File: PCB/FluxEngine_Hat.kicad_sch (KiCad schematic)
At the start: 6 parts, among them J1 CY8CKIT-059, P1 FDD_IBMPC_host, P2 FDD_SA800_host

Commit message: CDC pinouts
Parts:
- removed P1: FDD_IBMPC_host, 000_LOCAL:IDC-Header_2x17_P2.54mm_Latch_Vertical - FDD, symbol 000_LOCAL:FDD_IBMPC_host
- added P1: FDC_BUS_IBMPC, 000_LOCAL:IDC-Header_2x17_P2.54mm_Latch_Vertical - FDD, symbol 000_LOCAL:FDC_BUS_IBMPC
- P2: value FDD_SA800_host -> FDC_BUS_SA851; symbol 000_LOCAL:FDD_SA800_host -> 000_LOCAL:FDC_BUS_SA851
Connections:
- net DIR: now also P1.18 (DIR)
- net GND: now also P1.1 (GND), P1.11 (GND), P1.13 (GND), P1.15 (GND), P1.17 (GND), P1.19 (GND), P1.21 (GND), P1.23 (GND), P1.25 (GND), P1.27 (GND), P1.29 (GND), P1.31 (GND), P1.33 (GND), P1.7 (GND), P1.9 (GND)
- net SIDE: now also P1.32 (SIDE)
- net ~{DSA}: now also J1.J1_14 (12.2), P1.14 (~{DRVSA}); no longer J1.J1_13 (12.3), P2.26 (~{DS1})
- net ~{DSB}: now also J1.J1_13 (12.3), P2.26 (~{DS1}), P1.12 (~{DRVSB}); no longer J1.J1_14 (12.2)
- net ~{DSKCHG}: now also P1.34 (~{DSKCHG})
- net ~{INDEX}: now also P1.8 (~{INDEX})
- net ~{MOTA}: now also J1.J1_12 (12.4), P1.10 (~{MOTEA}); no longer J1.J1_15 (12.1), JP2.2 (B), JP3.2 (B)
- net ~{MOTB}: now also J1.J1_15 (12.1), JP2.2 (B), JP3.2 (B), P1.16 (~{MOTEB}); no longer J1.J1_12 (12.4)
- net ~{RDATA}: now also P1.30 (~{RDATA})
- net ~{REDWC}: now also P1.2 (~{REDWC})
- net ~{STEP}: now also P1.20 (~{STEP})
- net ~{TRK0}: now also P1.26 (~{TRK0})
- net ~{WDATA}: now also P1.22 (~{WDATA})
- net ~{WGATE}: now also P1.24 (~{WGATE})
- net ~{WPROT}: now also P1.28 (~{WPT})
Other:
- note added: "FluxEngine treats Drive-Select-B and Motor-On-B as "drive 0". PC drives are all configured to be "B:" drives, and rely on the cable twist to become "A:" drives. A normal PC drive connected directly to the FluxEngine with no twist will appear as "drive 0". For the 50-pin connector for 8-inch drives: Connect ~{DSB} from the FluxEngine to ~{DS1} on the drive. Connect ~{MOTB} from the FluxEngine to ~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"
- note added: "Supports Shugart SA800-851 and most other 8-inch drives, ex: YD-174 NOT for Control Data / Magnetic Peripherals!"
- note removed: "From the FluxEngine web site: "FluxEngine, sadly, uses non-standard disk numbering (there are reasons). Drive 0 is the one nearest the motherboard; that is, before the twist. Drive 1 is the one at the end of the cable; that is, after the twist. Drive 0 is the default." So MOTA DSA MOTB DSB are flipped here to reflect what they are at the FluxEngine, not what the FDC bus normally has, so that the 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"
- title: FluxEngine_Hat for PC and SA800 -> FluxEngine_Hat for PC and SA850
- moved on the sheet: P2

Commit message: schematic notes
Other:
- note added: "Supports Shugart SA800-851 and most other 8-inch drives."
- note removed: "Supports Shugart SA800-851 and most other 8-inch drives, ex: YD-174 NOT for Control Data / Magnetic Peripherals!"
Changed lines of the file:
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@@
 		)
 	)
-	(text "Supports Shugart SA800-851 and most other 8-inch drives, ex: YD-174\n\nNOT for Control Data / Magnetic Peripherals!"
+	(text "Supports Shugart SA800-851 and most other 8-inch drives."
 		(exclude_from_sim no)
 		(at 139.7 38.1 0)

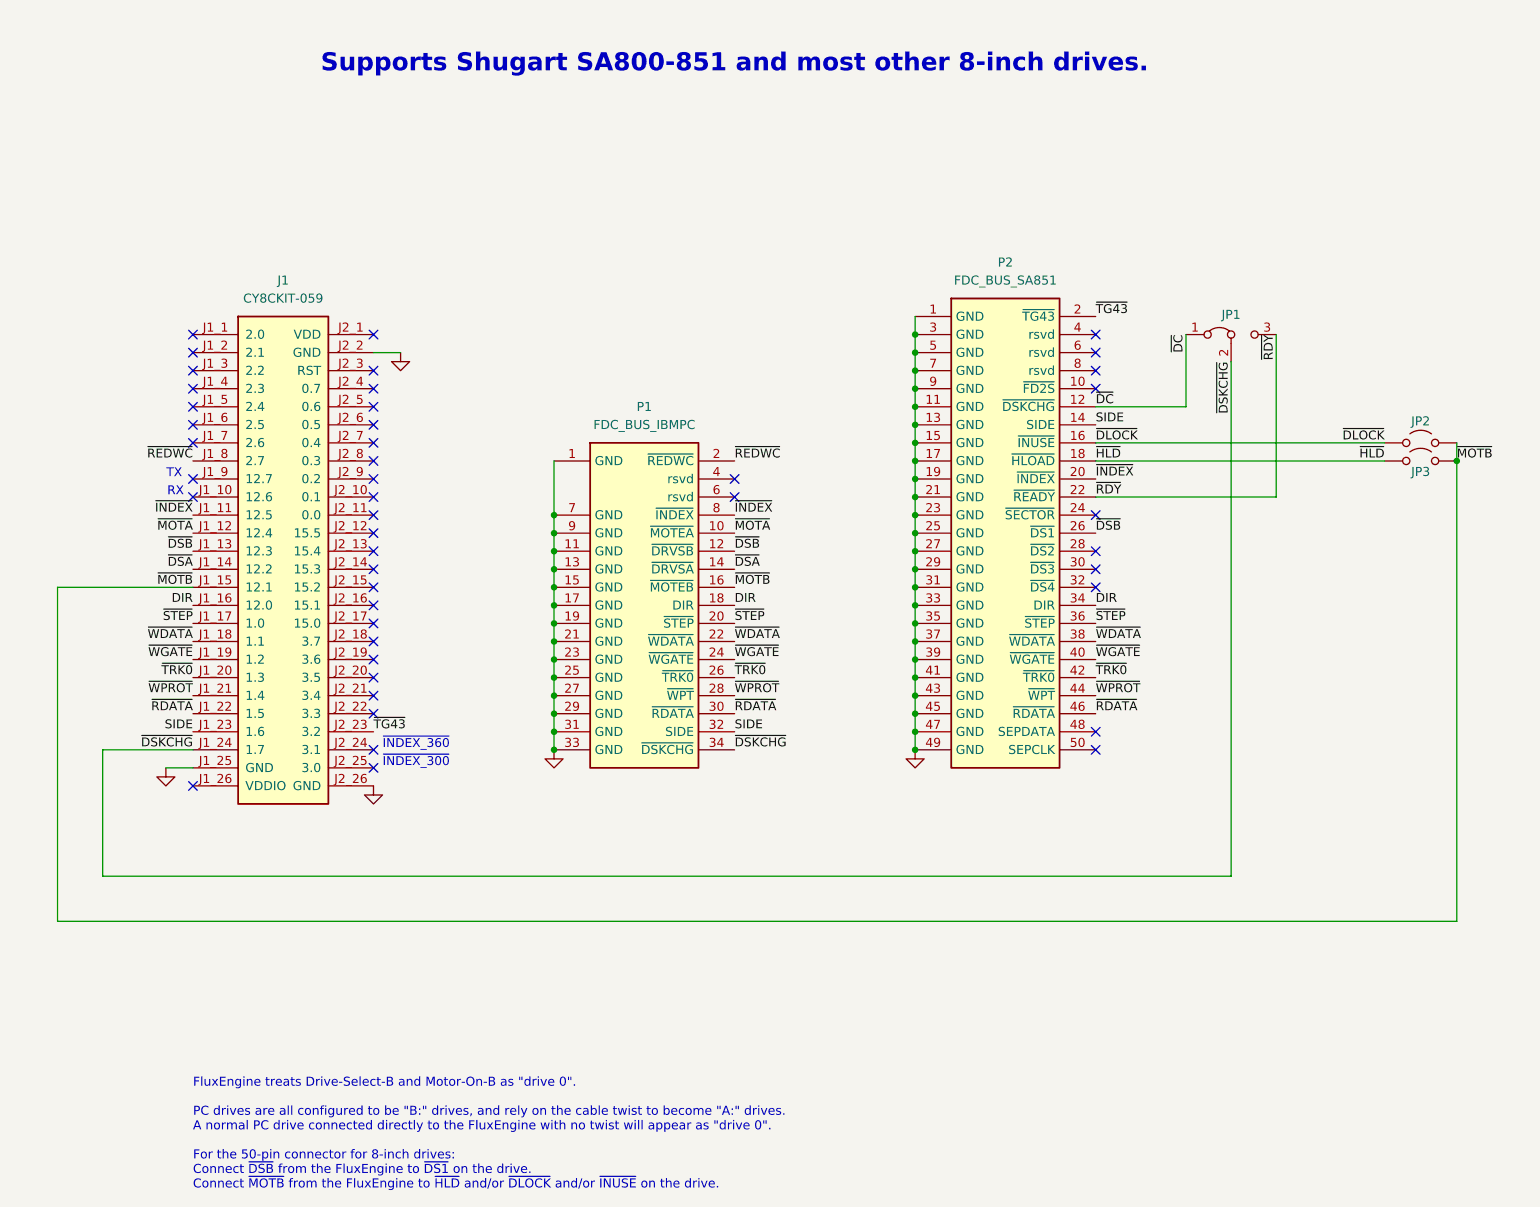
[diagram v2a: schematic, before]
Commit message: rotate 1G19 for easier hand soldering
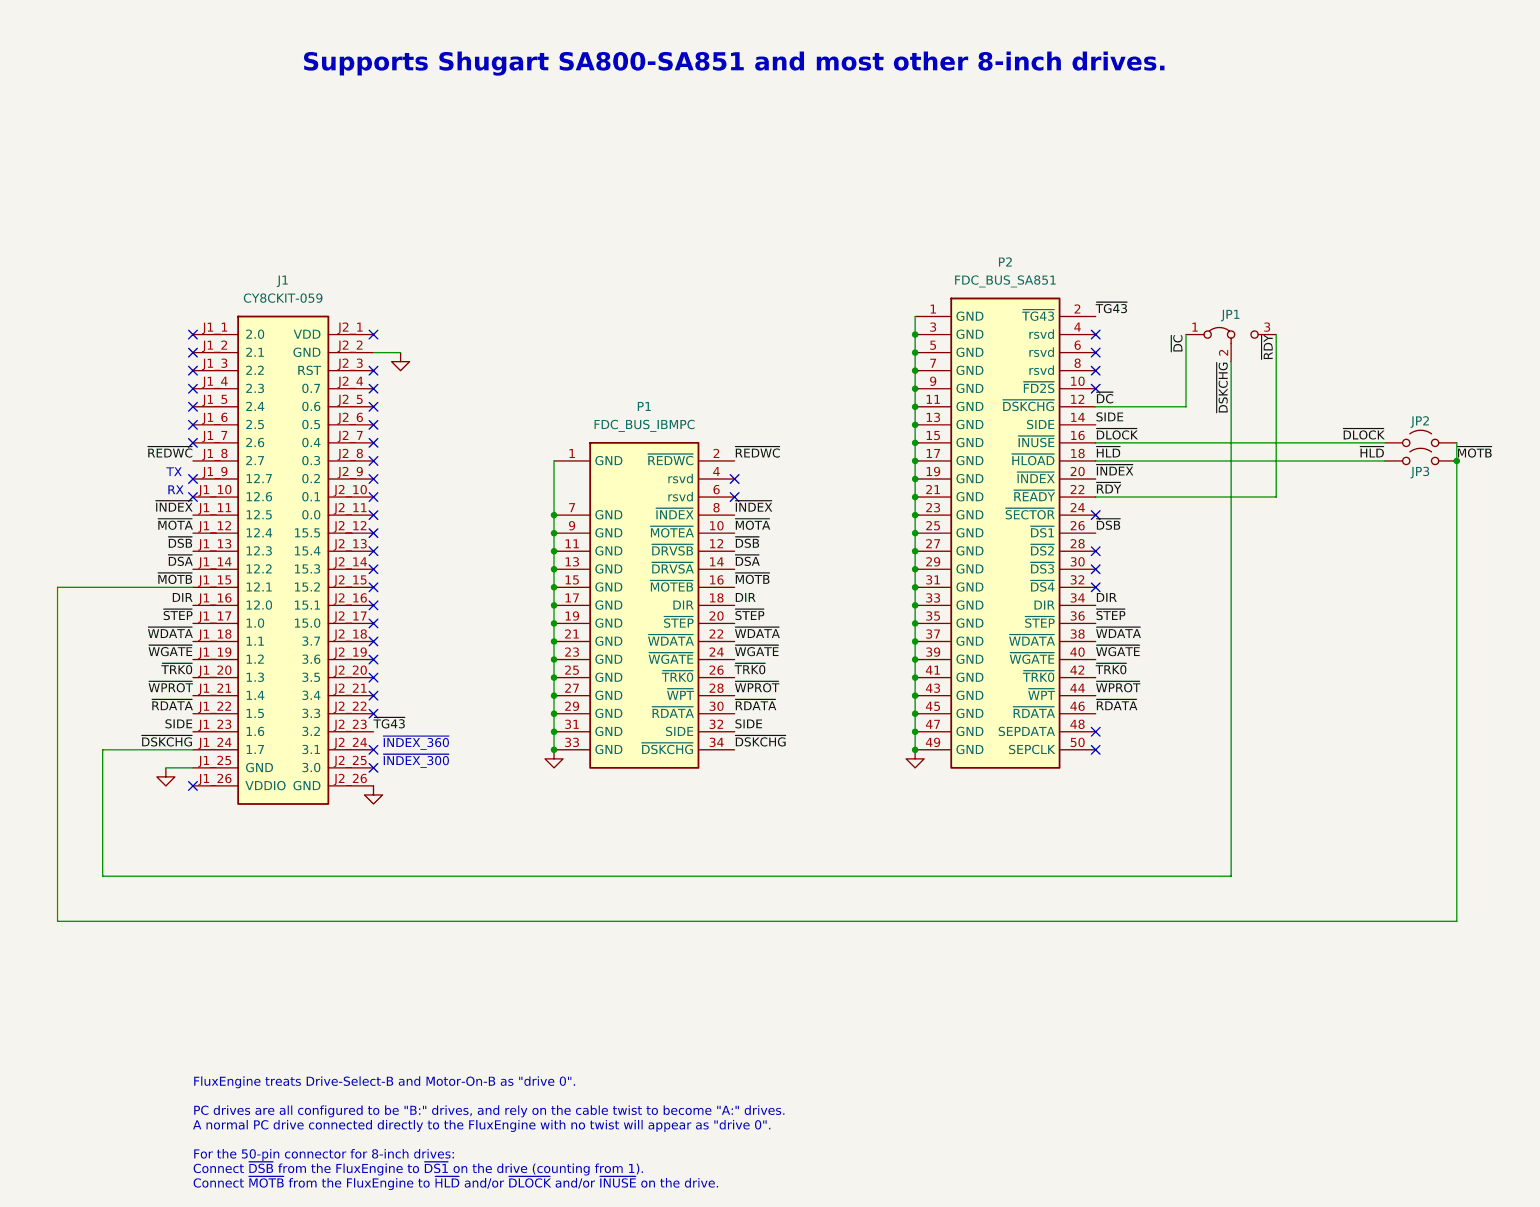
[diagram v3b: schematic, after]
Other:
- note added: "FluxEngine treats Drive-Select-B and Motor-On-B as "drive 0". PC drives are all configured to be "B:" drives, and rely on the cable twist to become "A:" drives. A normal PC drive connected directly to the FluxEngine with no twist will appear as "drive 0". For the 50-pin connector for 8-inch drives: Connect ~{DSB} from the FluxEngine to ~{DS1} on the drive (counting from 1). Connect ~{MOTB} from t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"
- note added: "Supports Shugart SA800-SA851 and most other 8-inch drives."
- note removed: "FluxEngine treats Drive-Select-B and Motor-On-B as "drive 0". PC drives are all configured to be "B:" drives, and rely on the cable twist to become "A:" drives. A normal PC drive connected directly to the FluxEngine with no twist will appear as "drive 0". For the 50-pin connector for 8-inch drives: Connect ~{DSB} from the FluxEngine to ~{DS1} on the drive. Connect ~{MOTB} from the FluxEngine to ~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"
- note removed: "Supports Shugart SA800-851 and most other 8-inch drives."
- title: FluxEngine_Hat for PC and SA850 -> FluxEngine_Hat for PC and Shugart
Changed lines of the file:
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@@
 	(paper "User" 298.45 217.322)
 	(title_block
-		(title "FluxEngine_Hat for PC and SA850")
-		(date "2024-04-25")
-		(rev "014")
+		(title "FluxEngine_Hat for PC and Shugart")
+		(date "2024-05-27")
+		(rev "015")
 		(company "Brian K. White - b.kenyon.w@gmail.com")
 		(comment 1 "CC BY-SA")
@@
 		)
 	)
-	(text "FluxEngine treats Drive-Select-B and Motor-On-B as \"drive 0\".\n\nPC drives are all configured to be \"B:\" drives, and rely on the cable twist to become \"A:\" drives.\nA normal PC drive connected directly to the FluxEngine with no twist will appear as \"drive 0\".\n\nFor the 50-pin connector for 8-inch drives:\nConnect ~{DSB} from the FluxEngine to ~{DS1} on the drive.\nConnect ~{MOTB} from the FluxEngine to ~{HLD} and/or ~{DLOCK} and/or ~{INUSE} on the drive.\n"
+	(text "FluxEngine treats Drive-Select-B and Motor-On-B as \"drive 0\".\n\nPC drives are all configured to be \"B:\" drives, and rely on the cable twist to become \"A:\" drives.\nA normal PC drive connected directly to the FluxEngine with no twist will appear as \"drive 0\".\n\nFor the 50-pin connector for 8-inch drives:\nConnect ~{DSB} from the FluxEngine to ~{DS1} on the drive (counting from 1).\nConnect ~{MOTB} from the FluxEngine to ~{HLD} and/or ~{DLOCK} and/or ~{INUSE} on the drive.\n"
 		(exclude_from_sim no)
 		(at 63.5 196.596 0)
@@
 		)
 	)
-	(text "Supports Shugart SA800-851 and most other 8-inch drives."
+	(text "Supports Shugart SA800-SA851 and most other 8-inch drives."
 		(exclude_from_sim no)
 		(at 139.7 38.1 0)
